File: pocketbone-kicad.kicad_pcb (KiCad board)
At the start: 2 copper layers, 55 x 35 mm, 63 parts, among them P1 USB_OTG, P2 USB_OTG, U1 SN74LVC1G07, U2 OSD3358, U3 24LC32AT-I/OT, U4 TPS2051C

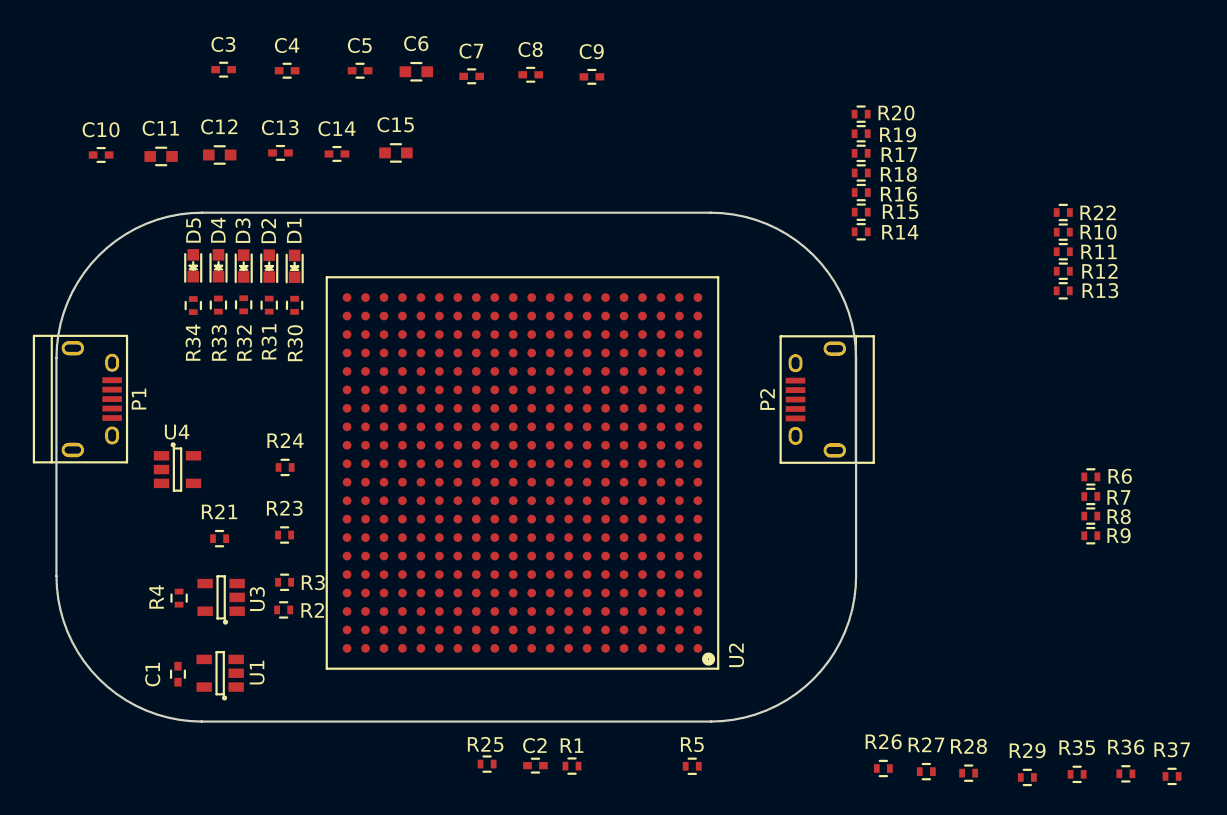
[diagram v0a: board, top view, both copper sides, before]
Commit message: Few PCB updates
Adds pattern for SD card and 24Mhz SMD crystal.
Removes 32.768KHz crystal from design.
Preliminary placement done.
Need to add test points.
All patterns need to be verified with specific components.

Signed-off-by: Michael Welling <mwelling@ieee.org>
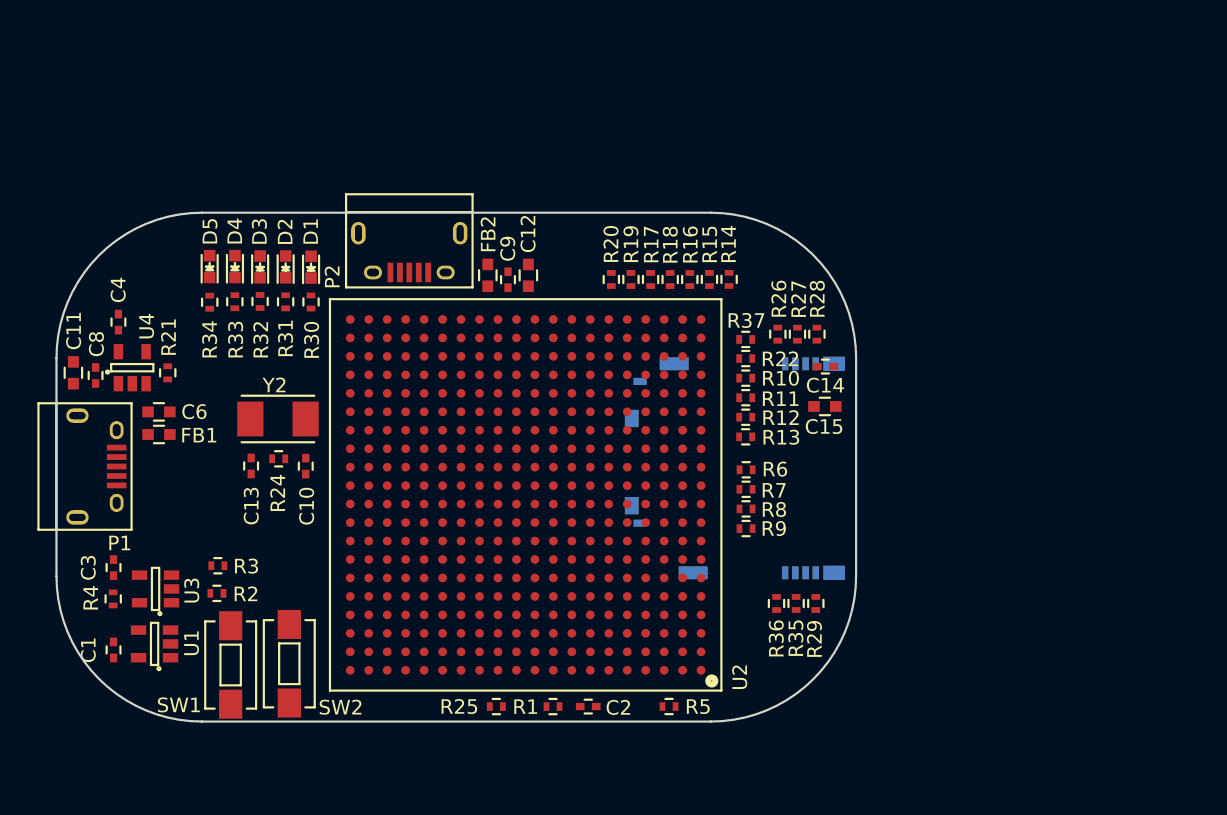
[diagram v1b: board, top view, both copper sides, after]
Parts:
- removed C5, C7: 18pF, Capacitors_SMD:C_0402
- removed R23: 1M, Resistors_SMD:R_0402
- added FB1: FILTER, Capacitors_SMD:C_0603, F.Cu at (113.0, 110.2)
- added FB2: FILTER, Capacitors_SMD:C_0603, F.Cu at (135.6, 99.2)
- added SOK1: SCHA5B0200, pocketbone-kicad:SCHA5B0200, B.Cu at (159.5, 112.5)
- added SW1: SW_PUSH_SMALL_H, Buttons_Switches_SMD:SW_SPST_EVQPE1, F.Cu at (117.9, 126.0)
- added SW2: SW_PUSH_SMALL_H, Buttons_Switches_SMD:SW_SPST_EVQPE1, F.Cu at (122.0, 126.0)
- added Y2: 24MHz, pocketbone-kicad:445C33D24M00000, F.Cu at (121.2, 109.1)
- moved R37 42.0 mm to (153.4, 103.6), turned to 180 degrees
- moved C14 36.6 mm to (158.9, 105.5)
- moved C8 36.4 mm to (108.7, 106.1), turned to 90 degrees
- moved C3 35.1 mm to (109.9, 119.3), turned to 90 degrees
- moved C15 34.3 mm to (158.8, 108.3)
- moved R28 31.9 mm to (158.3, 103.3), turned to 270 degrees
- moved R27 31.4 mm to (156.9, 103.3), turned to 270 degrees
- moved R26 30.7 mm to (155.6, 103.3), turned to 270 degrees
- moved P2 30.0 mm to (130.2, 97.5), turned to 180 degrees
- moved C6 29.3 mm to (113.0, 108.6)
- moved R36 26.7 mm to (155.5, 121.8), turned to 90 degrees
- moved C10 25.6 mm to (123.1, 112.4), turned to 270 degrees
- moved R11 24.0 mm to (153.4, 107.7), turned to 180 degrees
- moved R12 24.0 mm to (153.4, 109.0)
- moved R22 24.0 mm to (153.4, 105.0)
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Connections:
- U2 pad G20: OSC1_GND -> Net-(U2-PadG20)

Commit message: 2 layer routing attempt
TODO: Figure out proper USB routing with 2 layers.

Signed-off-by: Michael Welling <mwelling@ieee.org>
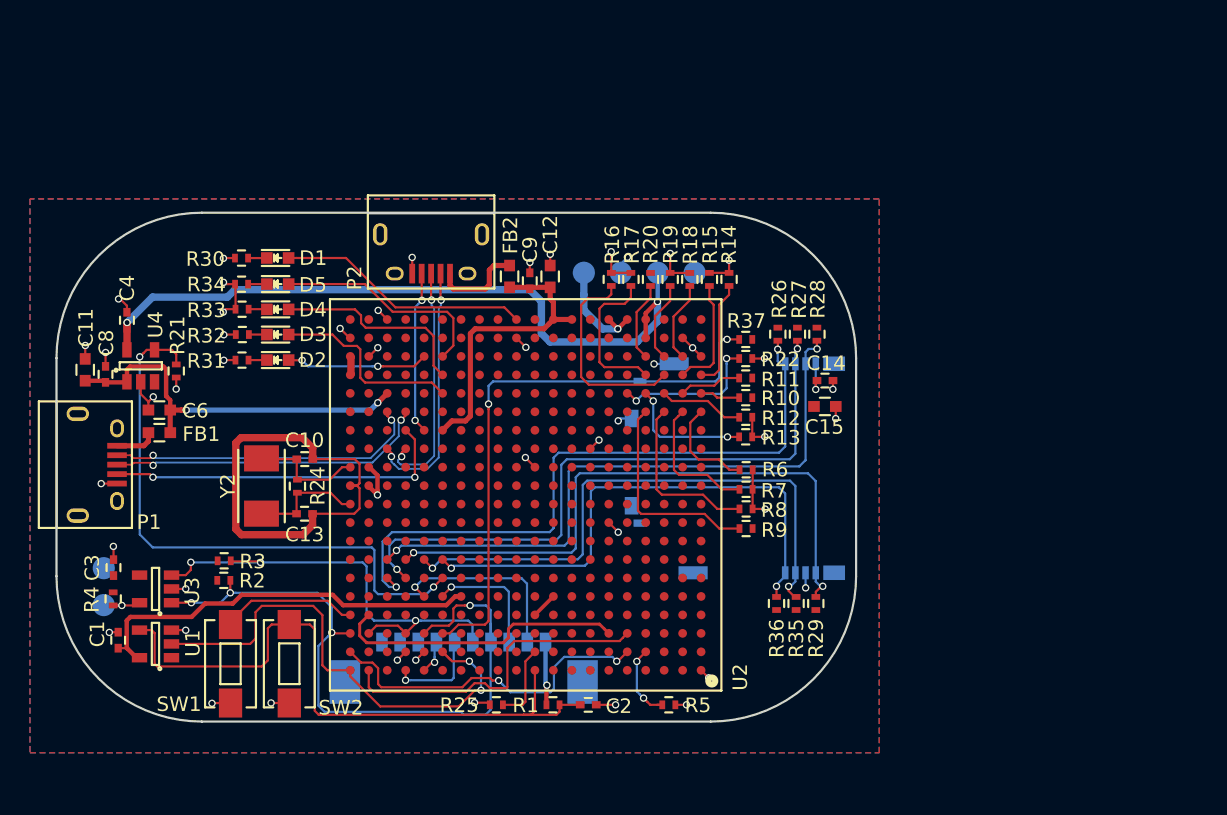
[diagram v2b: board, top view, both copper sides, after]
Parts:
- added P3: CONN_01X10, Connectors_Molex:Connector_Molex_PicoBlade_53398-1071, B.Cu at (134.0, 127.2)
- added TP1: 5V, Measurement_Points:Measurement_Point_Round-SMD-Pad_Small, B.Cu at (142.2, 99.1)
- added TP2: WP, Measurement_Points:Measurement_Point_Round-SMD-Pad_Small, B.Cu at (109.2, 121.9)
- added TP3: GND, Measurement_Points:Measurement_Point_Round-SMD-Pad_Small, B.Cu at (109.2, 119.4)
- added TP4: 3P3, Measurement_Points:Measurement_Point_Round-SMD-Pad_Small, B.Cu at (144.8, 99.1)
- added TP5: SYS_5V, Measurement_Points:Measurement_Point_Round-SMD-Pad_Small, B.Cu at (147.3, 99.1)
- added TP6: GND, Measurement_Points:Measurement_Point_Round-SMD-Pad_Small, B.Cu at (149.9, 99.1)
- moved D2 6.43 mm to (121.2, 105.1), turned to 0 degrees
- moved R30 5.65 mm to (118.7, 98.0), turned to 0 degrees
- moved R16 5.40 mm to (144.1, 99.5)
- moved R31 5.01 mm to (118.7, 105.1), turned to 0 degrees
- moved C13 4.93 mm to (123.0, 115.6), turned to 0 degrees
- moved D5 4.84 mm to (121.2, 99.8), turned to 0 degrees
- moved D3 4.81 mm to (121.2, 103.3), turned to 0 degrees
- moved Y2 4.75 mm to (120.1, 113.7), turned to 270 degrees
- moved D4 4.17 mm to (121.2, 101.6), turned to 0 degrees
- moved R19 2.70 mm to (148.2, 99.5)
- moved R20 2.69 mm to (146.8, 99.5)
- moved R32 2.58 mm to (118.8, 103.3), turned to 0 degrees
- moved R34 2.52 mm to (118.7, 99.8), turned to 0 degrees
- moved D1 2.38 mm to (121.2, 98.0), turned to 0 degrees
- moved R24 2.28 mm to (122.5, 113.7), turned to 90 degrees
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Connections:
- U2 pad A16: Net-(U2-PadA16) -> SPI_CS0
- U2 pad A17: Net-(U2-PadA17) -> SPI_CLK
- U2 pad B16: Net-(U2-PadB16) -> SPI_MOSI
- U2 pad B17: Net-(U2-PadB17) -> SPI_MISO
- U2 pad E15: Net-(U2-PadE15) -> UART0_RXD
- U2 pad E16: Net-(U2-PadE16) -> UART0_TXD
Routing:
- net GND: track 0.00 -> 57.0 mm, vias 0 -> 44
- net SYS_5V: track 0.00 -> 48.9 mm, vias 0 -> 2
- net I2C0_SCL: track 0.00 -> 47.4 mm, vias 0 -> 4
- net MMC0_DAT2: track 0.00 -> 45.6 mm, vias 0 -> 2
- net Net-(C2-Pad1): track 0.00 -> 45.2 mm
- net MMC0_DAT3: track 0.00 -> 43.9 mm, vias 0 -> 2
- net MMC0_CMD: track 0.00 -> 43.3 mm, vias 0 -> 2
- net MMC0_CLK: track 0.00 -> 42.3 mm, vias 0 -> 2
- net USB1_DRVVBUS: track 0.00 -> 40.4 mm, vias 0 -> 2
- net MMC0_CD: track 0.00 -> 39.6 mm, vias 0 -> 2
- net MMC0_DAT0: track 0.00 -> 39.4 mm, vias 0 -> 2
- net MMC0_DAT1: track 0.00 -> 36.4 mm, vias 0 -> 2
- net PMIC_PGOOD: track 0.00 -> 34.2 mm, vias 0 -> 2
- net I2C0_SDA: track 0.00 -> 32.4 mm, vias 0 -> 3
- net OSC0_GND: track 0.00 -> 29.8 mm
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- added copper zone on F.Cu, net +3V3
- added copper zone on B.Cu, net GND
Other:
- net class Default: clearance 0.2 -> 0.1524; trace_width 0.25 -> 0.1524; via_dia 0.6 -> 0.508; via_drill 0.4 -> 0.3302
- rule trace_clearance: 0.2 -> 0.1524
- rule trace_min: 0.2 -> 0.1524
- rule via_min_drill: 0.3 -> 0.3302
- rule via_min_size: 0.4 -> 0.508

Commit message: Pull back routing and update placement
The placement and footprint updated for USB.

TODO: Attempt single sided population.

Signed-off-by: Michael Welling <mwelling@ieee.org>
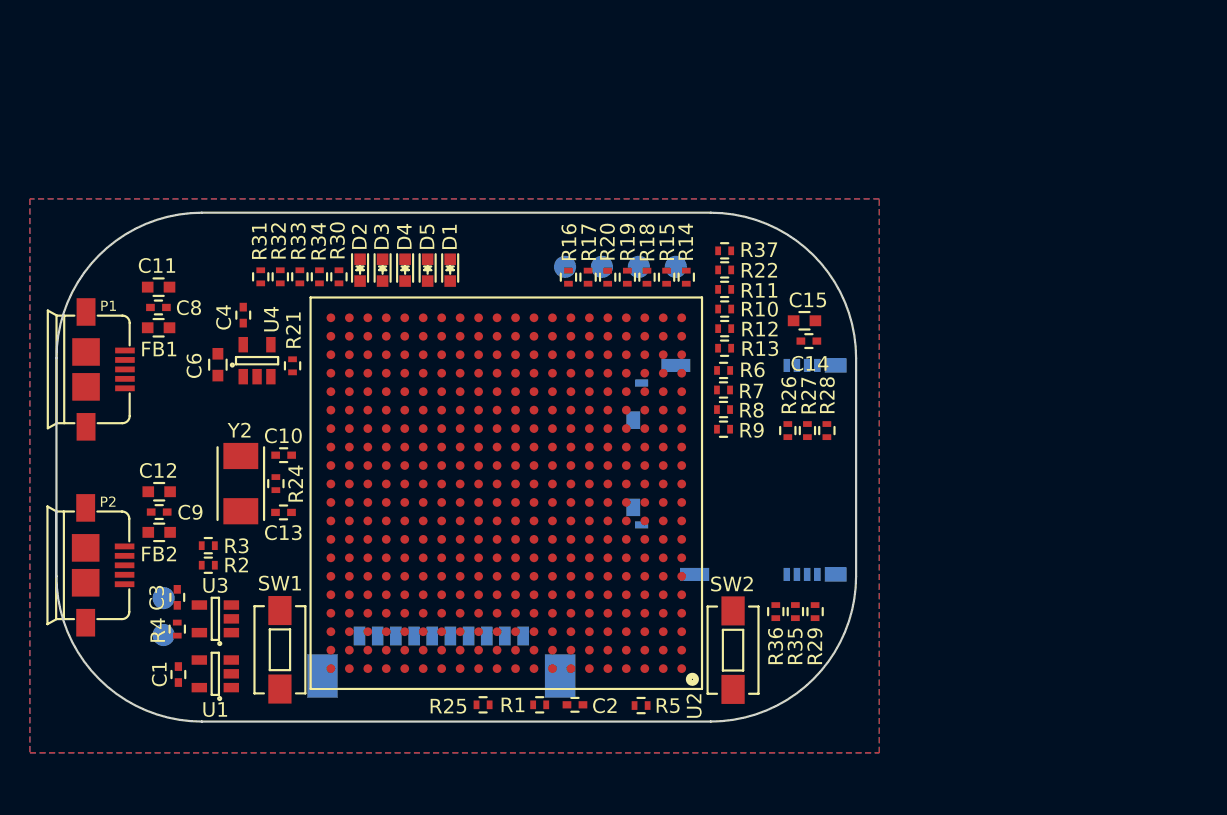
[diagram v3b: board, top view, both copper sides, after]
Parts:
- P1, P2: footprint Connect:USB_Micro-B -> Sensors:USB_MICRO_B_ST-USB-001E
- moved P2 33.3 mm to (106.5, 119.2), turned to 270 degrees
- moved C12 30.7 mm to (113.0, 114.1), turned to 180 degrees
- moved SW2 30.5 mm to (152.5, 125.0)
- moved C9 30.0 mm to (113.0, 115.5), turned to 180 degrees
- moved FB2 29.8 mm to (113.0, 116.9), turned to 180 degrees
- moved D1 11.9 mm to (133.0, 98.9), turned to 270 degrees
- moved D5 10.4 mm to (131.5, 98.9), turned to 270 degrees
- moved D4 9.16 mm to (129.9, 98.9), turned to 270 degrees
- moved D3 8.46 mm to (128.4, 98.9), turned to 270 degrees
- moved D2 8.38 mm to (126.8, 98.9), turned to 270 degrees
- moved C4 8.01 mm to (118.8, 102.0)
- moved R21 8.01 mm to (122.2, 105.5)
- moved U4 8.01 mm to (119.8, 105.1)
- moved C11 7.60 mm to (113.0, 100.1), turned to 180 degrees
- moved FB1 7.21 mm to (113.0, 102.8)
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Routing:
- net GND: track 57.0 -> 0.00 mm, vias 44 -> 0
- net SYS_5V: track 48.9 -> 0.00 mm, vias 2 -> 0
- net I2C0_SCL: track 47.4 -> 0.00 mm, vias 4 -> 0
- net MMC0_DAT2: track 45.6 -> 0.00 mm, vias 2 -> 0
- net Net-(C2-Pad1): track 45.2 -> 0.00 mm
- net MMC0_DAT3: track 43.9 -> 0.00 mm, vias 2 -> 0
- net MMC0_CMD: track 43.3 -> 0.00 mm, vias 2 -> 0
- net MMC0_CLK: track 42.3 -> 0.00 mm, vias 2 -> 0
- net USB1_DRVVBUS: track 40.4 -> 0.00 mm, vias 2 -> 0
- net MMC0_CD: track 39.6 -> 0.00 mm, vias 2 -> 0
- net MMC0_DAT0: track 39.4 -> 0.00 mm, vias 2 -> 0
- net MMC0_DAT1: track 36.4 -> 0.00 mm, vias 2 -> 0
- net PMIC_PGOOD: track 34.2 -> 0.00 mm, vias 2 -> 0
- net I2C0_SDA: track 32.4 -> 0.00 mm, vias 3 -> 0
- net OSC0_GND: track 29.8 -> 0.00 mm
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
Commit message: Many PCB updates
Updated the placement for single sided population.
Switched boot mode selection resistors to arrays to save space.
Switched expansion header to .1 inch (lichen pub compatible).
Added battery connect similar to BBB.

Signed-off-by: Michael Welling <mwelling@ieee.org>
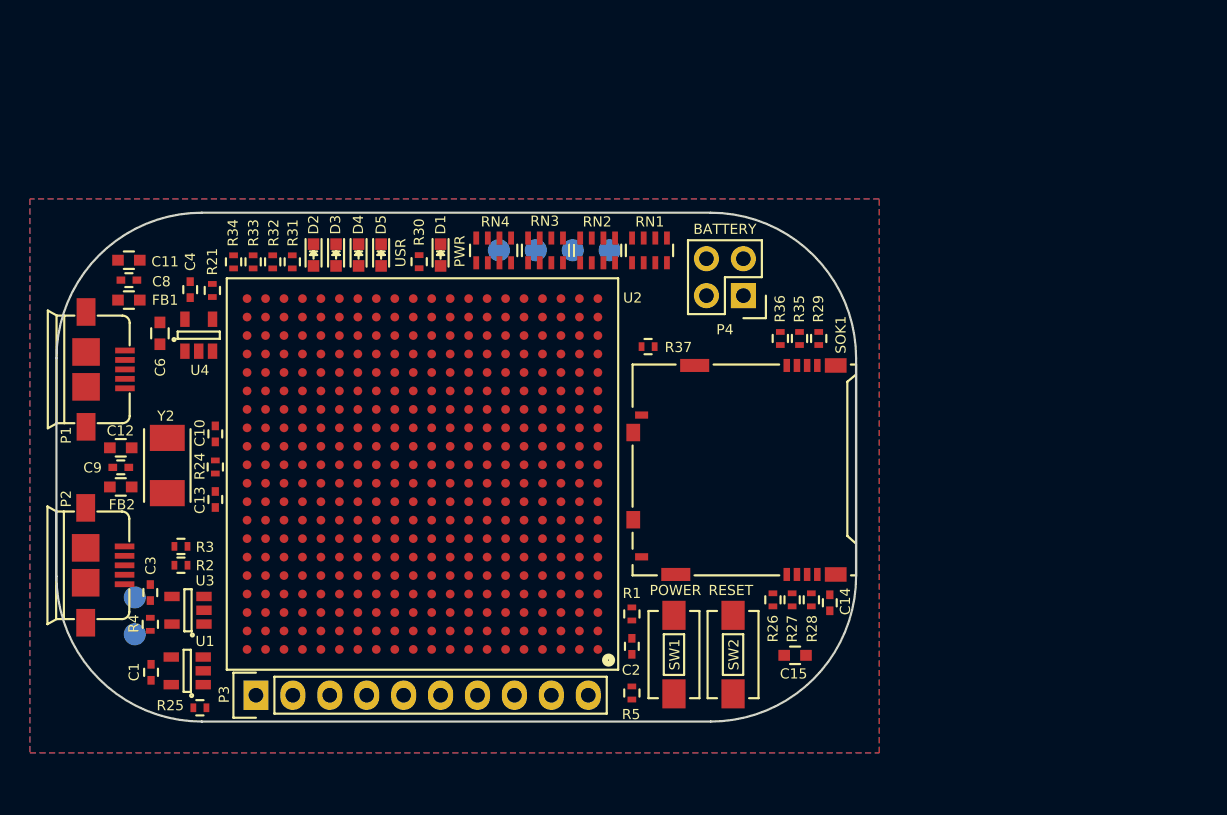
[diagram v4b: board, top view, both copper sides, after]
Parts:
- removed R10, R11, R12, R13, R14, R15, R16, R17, R18, R19, R20, R22, R6, R7, R8, R9: 100K, Resistors_SMD:R_0402
- added G***: LOGO, libs:boris, B.Cu at (151.1, 112.7)
- added G***: LOGO, libs:qwerty, B.Cu at (114.8, 112.7)
- added P4: CONN_02X02, Socket_Strips:Socket_Strip_Straight_2x02, F.Cu at (153.2, 100.6)
- added RN1: 100K, Resistors_SMD:R_Array_Concave_4x0603, F.Cu at (146.8, 97.5)
- added RN2: 100K, Resistors_SMD:R_Array_Concave_4x0603, F.Cu at (143.2, 97.5)
- added RN3: 100K, Resistors_SMD:R_Array_Concave_4x0603, F.Cu at (139.6, 97.5)
- added RN4: 100K, Resistors_SMD:R_Array_Concave_4x0603, F.Cu at (136.0, 97.5)
- P3: footprint Connectors_Molex:Connector_Molex_PicoBlade_53398-1071 -> Socket_Strips:Socket_Strip_Straight_1x10; moved to F.Cu
- SOK1: moved to F.Cu
- moved SW1 27.1 mm to (148.4, 125.3)
- moved C15 23.0 mm to (156.8, 125.4)
- moved R25 19.5 mm to (115.8, 129.0)
- moved R36 18.8 mm to (155.8, 103.6), turned to 270 degrees
- moved R29 18.8 mm to (158.4, 103.6), turned to 270 degrees
- moved R35 18.8 mm to (157.1, 103.6), turned to 270 degrees
- moved C14 18.1 mm to (159.2, 121.8), turned to 270 degrees
- moved P3 12.8 mm to (119.7, 128.1), turned to 0 degrees
- moved R28 11.7 mm to (157.9, 121.6), turned to 90 degrees
- moved R27 11.7 mm to (156.6, 121.6), turned to 90 degrees
- moved R26 11.7 mm to (155.2, 121.6), turned to 90 degrees
- moved R1 8.90 mm to (145.5, 122.5), turned to 270 degrees
- moved R37 8.43 mm to (146.7, 104.1)
- moved R21 7.57 mm to (116.7, 100.3)
- moved R34 6.00 mm to (118.1, 98.3), turned to 90 degrees
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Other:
- board text added: "+3V3"
- board text added: "+5V"
- board text added: "BATTERY"
- board text added: "GND"
- board text added: "I2C0_SCL"
- board text added: "I2C0_SDA"
- board text added: "POWER"
- board text added: "PWR"
- board text added: "RESET"
- board text added: "SPI0_CS0"
- board text added: "SPI0_MISO"
- board text added: "SPI0_MOSI"
- board text added: "SPI0_SCLK"
- board text added: "SYS_5V"
- board text added: "UART0_RXD"
- board text added: "UART0_TXD"
- board text added: "USR"
- board text added: "WP"
